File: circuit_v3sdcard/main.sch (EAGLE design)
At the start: 24 parts, among them CN1 SD, CN3 MICROSD, CN4 5035481020, IC1 C8051F381-GM, IC3 N25Q512A, IC4 KC2016K, IC6 MPU-9250

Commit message: Modified v3 circuit
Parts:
- removed D1, D2: (no value), diode:DIODE-SOD323-W
- removed LED1: (no value), LED:LED1608O
- removed R7: 10k, reg,cap:R-1005
- removed TP: PTR1TP10R, testpad:PTR1TP10R
- removed USB_GND: PTR1TP11R, testpad:PTR1TP11R
- D4: value (none) -> HSMS-2854; device diode:DIODE-SOD323-W -> avago:HSMS-2854
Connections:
- removed net N$15: IC1G$1.P2.7, R7.P$2, TP.TP
- removed net N$4: D1.C, D2.C, IC1G$1.REGIN
- removed net N$5: D4.C, IC1G$1.VBUS, R1.P$2
- removed net N$9: LED1.A, R7.P$1
- new net N$1: D4.C, IC1G$1.REGIN
- net +3V3: now also D4.A2; no longer D2.A
- net DGND: no longer LED1.K, USB_GND.TP
- net VBUS: now also D4.A1, IC1G$1.VBUS, R1.P$2; no longer D1.A, D4.A
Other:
- moved on the sheet: R1

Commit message: Fix parts positions
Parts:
- added C1: 1.0u, reg,cap:C-1005
- added R3: 100, reg,cap:R-1005
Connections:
- new net N$4: IC1G$1.VBUS, R3.P$1
- net DGND: now also C1.P$1
- net N$1: now also C1.P$2
- net VBUS: now also R3.P$2; no longer IC1G$1.VBUS
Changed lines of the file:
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@@
 <part name="SUPPLY1" library="supply2" deviceset="DGND" device=""/>
 <part name="D4" library="avago" library_urn="urn:adsk.eagle:library:107" deviceset="HSMS-2854" device="" package3d_urn="urn:adsk.eagle:package:4488/1"/>
+<part name="R3" library="reg,cap" deviceset="R-" device="1005" value="100"/>
+<part name="C1" library="reg,cap" deviceset="C-" device="1005" value="1.0u"/>
 </parts>
 <sheets>
@@
 <instance part="SUPPLY1" gate="G$1" x="-210.82" y="-60.96"/>
 <instance part="D4" gate="A" x="-48.26" y="-2.54" rot="MR180"/>
+<instance part="R3" gate="G$1" x="-40.64" y="-7.62" rot="R180"/>
+<instance part="C1" gate="G$1" x="-25.4" y="-22.86" rot="R90"/>
 </instances>
 <busses>
@@
 <pinref part="SUPPLY6" gate="G$1" pin="DGND"/>
 <pinref part="C6" gate="G$1" pin="P$1"/>
+<pinref part="C1" gate="G$1" pin="P$1"/>
+<wire x1="-30.48" y1="-27.94" x2="-25.4" y2="-27.94" width="0.1524" layer="91"/>
+<wire x1="-25.4" y1="-27.94" x2="-25.4" y2="-25.4" width="0.1524" layer="91"/>
 </segment>
 <segment>
@@
 <wire x1="-223.52" y1="-40.64" x2="-236.22" y2="-40.64" width="0.1524" layer="91"/>
 <label x="-233.68" y="-40.64" size="1.778" layer="95"/>
-<pinref part="IC1" gate="G$1" pin="VBUS"/>
 <pinref part="D3" gate="G$1" pin="4"/>
 <wire x1="-109.22" y1="-7.62" x2="-109.22" y2="-12.7" width="0.1524" layer="91"/>
@@
 <wire x1="-55.88" y1="-2.54" x2="-55.88" y2="-7.62" width="0.1524" layer="91"/>
 <junction x="-55.88" y="-7.62"/>
-<wire x1="-55.88" y1="-7.62" x2="-22.86" y2="-7.62" width="0.1524" layer="91"/>
+<wire x1="-55.88" y1="-7.62" x2="-45.72" y2="-7.62" width="0.1524" layer="91"/>
 <wire x1="-129.54" y1="-7.62" x2="-109.22" y2="-7.62" width="0.1524" layer="91"/>
 <junction x="-109.22" y="-7.62"/>
+<pinref part="R3" gate="G$1" pin="P$2"/>
 </segment>
 </net>
@@
 <pinref part="IC1" gate="G$1" pin="REGIN"/>
 <pinref part="D4" gate="A" pin="C"/>
-<wire x1="-48.26" y1="-5.08" x2="-22.86" y2="-5.08" width="0.1524" layer="91"/>
-</segment>
-</net>
+<wire x1="-48.26" y1="-5.08" x2="-25.4" y2="-5.08" width="0.1524" layer="91"/>
+<pinref part="C1" gate="G$1" pin="P$2"/>
+<wire x1="-25.4" y1="-5.08" x2="-22.86" y2="-5.08" width="0.1524" layer="91"/>
+<wire x1="-25.4" y1="-17.78" x2="-25.4" y2="-5.08" width="0.1524" layer="91"/>
+<junction x="-25.4" y="-5.08"/>
+</segment>
+</net>
+<net name="N$4" class="1">
+<segment>
+<pinref part="IC1" gate="G$1" pin="VBUS"/>
+<pinref part="R3" gate="G$1" pin="P$1"/>
+<wire x1="-38.1" y1="-7.62" x2="-22.86" y2="-7.62" width="0.1524" layer="91"/>
+</segment>
+</net>

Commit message: Added wiring
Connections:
- net D+: now also CN4.4; no longer CN4.6
- net D-: now also CN4.6; no longer CN4.4
- net GPIO0: now also IC1G$1.P2.6; no longer IC1G$1.P1.0
- net GPIO1: now also IC1G$1.P2.7; no longer IC1G$1.P1.1
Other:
- moved on the sheet: CN4

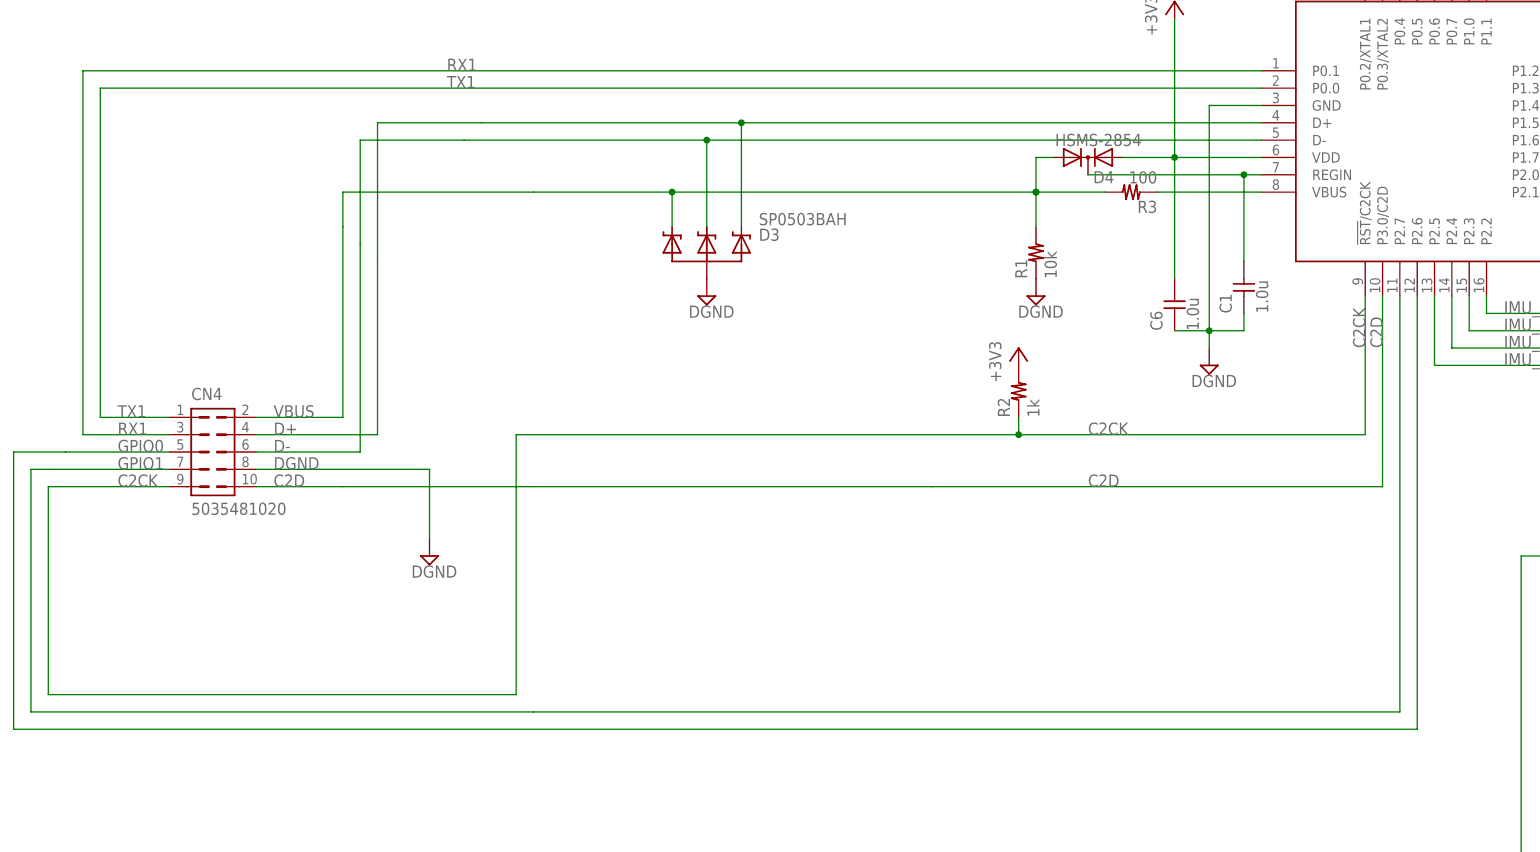
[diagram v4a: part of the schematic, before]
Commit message: Connected air wires
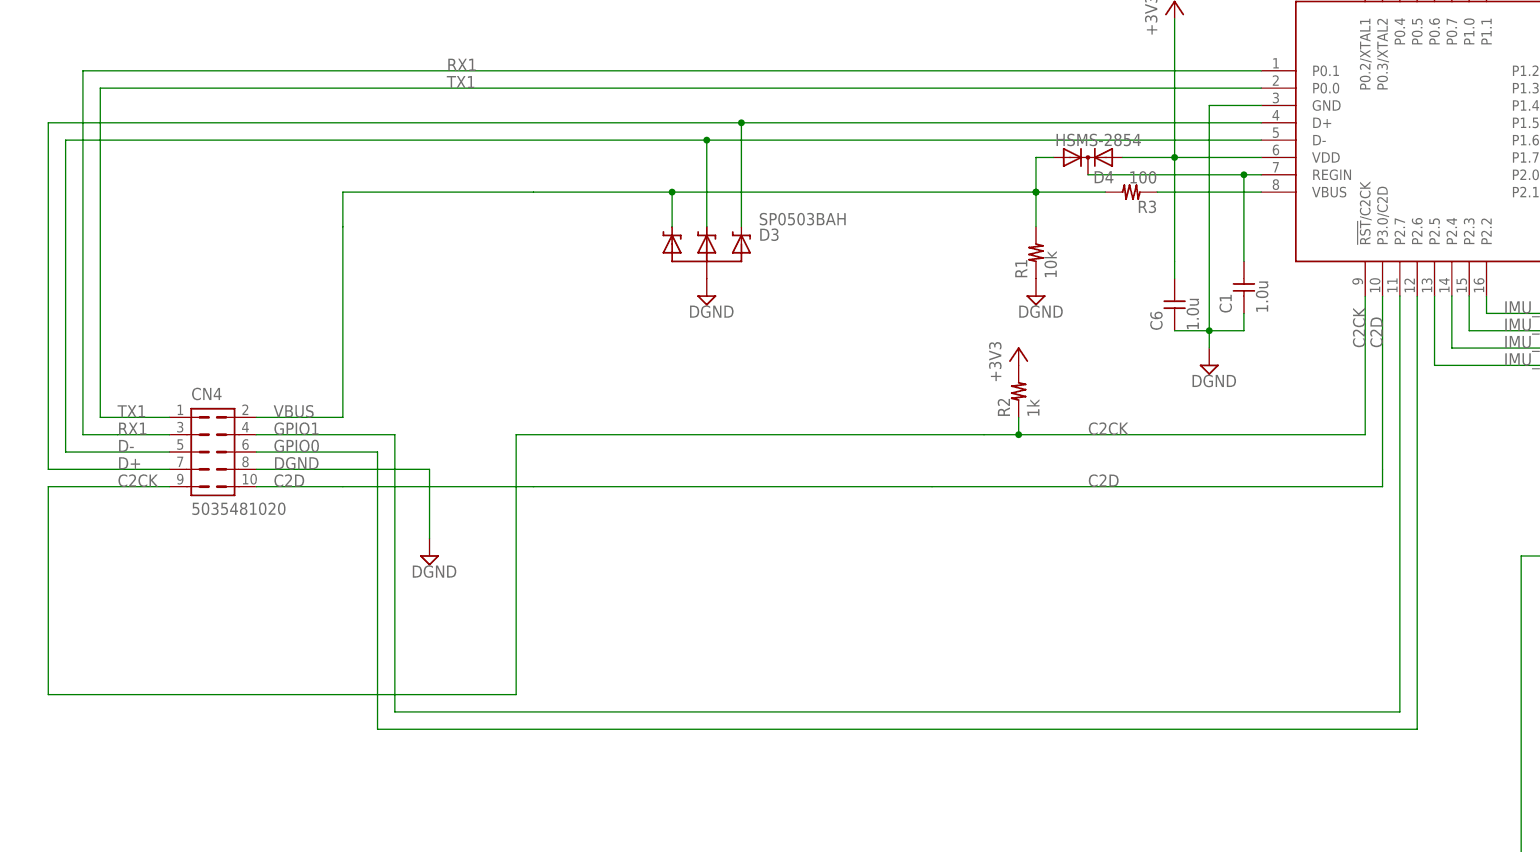
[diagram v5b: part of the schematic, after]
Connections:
- net D+: now also CN4.7; no longer CN4.4
- net D-: now also CN4.5; no longer CN4.6
- net GPIO0: now also CN4.6; no longer CN4.5
- net GPIO1: now also CN4.4; no longer CN4.7
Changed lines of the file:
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@@
 <segment>
 <wire x1="-22.86" y1="0" x2="-104.14" y2="0" width="0.1524" layer="91"/>
-<wire x1="-104.14" y1="0" x2="-139.7" y2="0" width="0.1524" layer="91"/>
-<wire x1="-154.94" y1="0" x2="-139.7" y2="0" width="0.1524" layer="91"/>
+<wire x1="-104.14" y1="0" x2="-198.12" y2="0" width="0.1524" layer="91"/>
 <wire x1="-104.14" y1="-12.7" x2="-104.14" y2="0" width="0.1524" layer="91"/>
 <junction x="-104.14" y="0"/>
 <pinref part="IC1" gate="G$1" pin="D-"/>
 <pinref part="D3" gate="G$1" pin="3"/>
-<wire x1="-154.94" y1="-43.18" x2="-154.94" y2="-15.24" width="0.1524" layer="91"/>
-<wire x1="-154.94" y1="-15.24" x2="-154.94" y2="0" width="0.1524" layer="91"/>
-<label x="-167.64" y="-45.72" size="1.778" layer="95"/>
-<wire x1="-154.94" y1="-43.18" x2="-154.94" y2="-45.72" width="0.1524" layer="91"/>
-<pinref part="CN4" gate="G$1" pin="6"/>
-<wire x1="-154.94" y1="-45.72" x2="-170.18" y2="-45.72" width="0.1524" layer="91"/>
+<label x="-190.5" y="-45.72" size="1.778" layer="95"/>
+<wire x1="-198.12" y1="0" x2="-198.12" y2="-45.72" width="0.1524" layer="91"/>
+<pinref part="CN4" gate="G$1" pin="5"/>
+<wire x1="-198.12" y1="-45.72" x2="-182.88" y2="-45.72" width="0.1524" layer="91"/>
 </segment>
 </net>
 <net name="D+" class="0">
 <segment>
-<wire x1="-137.16" y1="2.54" x2="-99.06" y2="2.54" width="0.1524" layer="91"/>
+<wire x1="-200.66" y1="2.54" x2="-99.06" y2="2.54" width="0.1524" layer="91"/>
 <wire x1="-99.06" y1="2.54" x2="-22.86" y2="2.54" width="0.1524" layer="91"/>
 <wire x1="-99.06" y1="-12.7" x2="-99.06" y2="2.54" width="0.1524" layer="91"/>
-<wire x1="-137.16" y1="2.54" x2="-152.4" y2="2.54" width="0.1524" layer="91"/>
 <junction x="-99.06" y="2.54"/>
 <pinref part="IC1" gate="G$1" pin="D+"/>
 <pinref part="D3" gate="G$1" pin="2"/>
-<wire x1="-152.4" y1="2.54" x2="-152.4" y2="-17.78" width="0.1524" layer="91"/>
-<wire x1="-152.4" y1="-17.78" x2="-152.4" y2="-43.18" width="0.1524" layer="91"/>
-<label x="-167.64" y="-43.18" size="1.778" layer="95"/>
-<pinref part="CN4" gate="G$1" pin="4"/>
-<wire x1="-170.18" y1="-43.18" x2="-152.4" y2="-43.18" width="0.1524" layer="91"/>
+<pinref part="CN4" gate="G$1" pin="7"/>
+<wire x1="-200.66" y1="2.54" x2="-200.66" y2="-48.26" width="0.1524" layer="91"/>
+<wire x1="-200.66" y1="-48.26" x2="-182.88" y2="-48.26" width="0.1524" layer="91"/>
+<label x="-190.5" y="-48.26" size="1.778" layer="95"/>
 </segment>
 </net>
@@
 <net name="GPIO0" class="0">
 <segment>
-<pinref part="CN4" gate="G$1" pin="5"/>
-<wire x1="-198.12" y1="-45.72" x2="-182.88" y2="-45.72" width="0.1524" layer="91"/>
-<label x="-190.5" y="-45.72" size="1.778" layer="95"/>
+<label x="-167.64" y="-45.72" size="1.778" layer="95"/>
 <pinref part="IC1" gate="G$1" pin="P2.6"/>
 <wire x1="0" y1="-22.86" x2="0" y2="-86.36" width="0.1524" layer="91"/>
-<wire x1="0" y1="-86.36" x2="-205.74" y2="-86.36" width="0.1524" layer="91"/>
-<wire x1="-205.74" y1="-86.36" x2="-205.74" y2="-45.72" width="0.1524" layer="91"/>
-<wire x1="-205.74" y1="-45.72" x2="-198.12" y2="-45.72" width="0.1524" layer="91"/>
+<wire x1="0" y1="-86.36" x2="-152.4" y2="-86.36" width="0.1524" layer="91"/>
+<pinref part="CN4" gate="G$1" pin="6"/>
+<wire x1="-152.4" y1="-86.36" x2="-152.4" y2="-45.72" width="0.1524" layer="91"/>
+<wire x1="-152.4" y1="-45.72" x2="-170.18" y2="-45.72" width="0.1524" layer="91"/>
 </segment>
 </net>
 <net name="GPIO1" class="0">
 <segment>
-<pinref part="CN4" gate="G$1" pin="7"/>
-<wire x1="-182.88" y1="-48.26" x2="-200.66" y2="-48.26" width="0.1524" layer="91"/>
-<label x="-190.5" y="-48.26" size="1.778" layer="95"/>
-<wire x1="-200.66" y1="-48.26" x2="-203.2" y2="-48.26" width="0.1524" layer="91"/>
-<wire x1="-203.2" y1="-48.26" x2="-203.2" y2="-83.82" width="0.1524" layer="91"/>
-<wire x1="-203.2" y1="-83.82" x2="-129.54" y2="-83.82" width="0.1524" layer="91"/>
+<label x="-167.64" y="-43.18" size="1.778" layer="95"/>
 <pinref part="IC1" gate="G$1" pin="P2.7"/>
-<wire x1="-129.54" y1="-83.82" x2="-2.54" y2="-83.82" width="0.1524" layer="91"/>
+<wire x1="-149.86" y1="-83.82" x2="-2.54" y2="-83.82" width="0.1524" layer="91"/>
 <wire x1="-2.54" y1="-83.82" x2="-2.54" y2="-22.86" width="0.1524" layer="91"/>
+<pinref part="CN4" gate="G$1" pin="4"/>
+<wire x1="-149.86" y1="-83.82" x2="-149.86" y2="-43.18" width="0.1524" layer="91"/>
+<wire x1="-149.86" y1="-43.18" x2="-170.18" y2="-43.18" width="0.1524" layer="91"/>
 </segment>
 </net>

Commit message: Modified circuit
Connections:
- net D+: now also CN4.5; no longer CN4.7
- net D-: now also CN4.3; no longer CN4.5
- net DGND: now also CN4.7; no longer CN4.8
- net GPIO0: now also CN4.8; no longer CN4.6
- net GPIO1: now also CN4.6; no longer CN4.4
- net RX1: now also CN4.4; no longer CN4.3
- net TX1: now also CN4.2; no longer CN4.1
- net VBUS: now also CN4.1; no longer CN4.2
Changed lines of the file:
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@@
 <instance part="R1" gate="G$1" x="-55.88" y="-17.78" rot="R90"/>
 <instance part="SUPPLY3" gate="G$1" x="-55.88" y="-22.86"/>
-<instance part="SUPPLY1" gate="G$1" x="-144.78" y="-60.96"/>
+<instance part="SUPPLY1" gate="G$1" x="-218.44" y="-50.8"/>
 <instance part="D4" gate="A" x="-48.26" y="-2.54" rot="MR180"/>
 <instance part="R3" gate="G$1" x="-40.64" y="-7.62" rot="R180"/>
@@
 </segment>
 <segment>
-<pinref part="CN4" gate="G$1" pin="8"/>
-<wire x1="-170.18" y1="-48.26" x2="-144.78" y2="-48.26" width="0.1524" layer="91"/>
-<wire x1="-144.78" y1="-48.26" x2="-144.78" y2="-58.42" width="0.1524" layer="91"/>
 <pinref part="SUPPLY1" gate="G$1" pin="DGND"/>
-<label x="-167.64" y="-48.26" size="1.778" layer="95"/>
+<label x="-190.5" y="-40.64" size="1.778" layer="95"/>
+<pinref part="CN4" gate="G$1" pin="7"/>
+<wire x1="-182.88" y1="-48.26" x2="-218.44" y2="-48.26" width="0.1524" layer="91"/>
 </segment>
 </net>
@@
 <pinref part="IC1" gate="G$1" pin="D-"/>
 <pinref part="D3" gate="G$1" pin="3"/>
-<label x="-190.5" y="-45.72" size="1.778" layer="95"/>
-<wire x1="-198.12" y1="0" x2="-198.12" y2="-45.72" width="0.1524" layer="91"/>
-<pinref part="CN4" gate="G$1" pin="5"/>
-<wire x1="-198.12" y1="-45.72" x2="-182.88" y2="-45.72" width="0.1524" layer="91"/>
+<label x="-190.5" y="-43.18" size="1.778" layer="95"/>
+<wire x1="-198.12" y1="0" x2="-198.12" y2="-43.18" width="0.1524" layer="91"/>
+<pinref part="CN4" gate="G$1" pin="3"/>
+<wire x1="-198.12" y1="-43.18" x2="-182.88" y2="-43.18" width="0.1524" layer="91"/>
 </segment>
 </net>
@@
 <pinref part="IC1" gate="G$1" pin="D+"/>
 <pinref part="D3" gate="G$1" pin="2"/>
-<pinref part="CN4" gate="G$1" pin="7"/>
-<wire x1="-200.66" y1="2.54" x2="-200.66" y2="-48.26" width="0.1524" layer="91"/>
-<wire x1="-200.66" y1="-48.26" x2="-182.88" y2="-48.26" width="0.1524" layer="91"/>
-<label x="-190.5" y="-48.26" size="1.778" layer="95"/>
+<wire x1="-200.66" y1="2.54" x2="-200.66" y2="-45.72" width="0.1524" layer="91"/>
+<label x="-190.5" y="-45.72" size="1.778" layer="95"/>
+<pinref part="CN4" gate="G$1" pin="5"/>
+<wire x1="-200.66" y1="-45.72" x2="-182.88" y2="-45.72" width="0.1524" layer="91"/>
 </segment>
 </net>
@@
 <net name="VBUS" class="1">
 <segment>
-<wire x1="-129.54" y1="-7.62" x2="-157.48" y2="-7.62" width="0.1524" layer="91"/>
-<wire x1="-157.48" y1="-7.62" x2="-157.48" y2="-12.7" width="0.1524" layer="91"/>
-<wire x1="-157.48" y1="-12.7" x2="-157.48" y2="-40.64" width="0.1524" layer="91"/>
-<pinref part="CN4" gate="G$1" pin="2"/>
-<wire x1="-157.48" y1="-40.64" x2="-170.18" y2="-40.64" width="0.1524" layer="91"/>
-<label x="-167.64" y="-40.64" size="1.778" layer="95"/>
+<wire x1="-109.22" y1="-7.62" x2="-157.48" y2="-7.62" width="0.1524" layer="91"/>
+<wire x1="-157.48" y1="-7.62" x2="-157.48" y2="-38.1" width="0.1524" layer="91"/>
+<label x="-190.5" y="-48.26" size="1.778" layer="95"/>
 <pinref part="D3" gate="G$1" pin="4"/>
 <wire x1="-109.22" y1="-7.62" x2="-109.22" y2="-12.7" width="0.1524" layer="91"/>
@@
 <junction x="-55.88" y="-7.62"/>
 <wire x1="-55.88" y1="-7.62" x2="-45.72" y2="-7.62" width="0.1524" layer="91"/>
-<wire x1="-129.54" y1="-7.62" x2="-109.22" y2="-7.62" width="0.1524" layer="91"/>
 <junction x="-109.22" y="-7.62"/>
 <pinref part="R3" gate="G$1" pin="P$2"/>
+<pinref part="CN4" gate="G$1" pin="1"/>
+<wire x1="-182.88" y1="-38.1" x2="-157.48" y2="-38.1" width="0.1524" layer="91"/>
+<wire x1="-182.88" y1="-40.64" x2="-182.88" y2="-38.1" width="0.1524" layer="91"/>
 </segment>
 </net>
@@
 <pinref part="IC1" gate="G$1" pin="P0.1"/>
 <wire x1="-22.86" y1="10.16" x2="-195.58" y2="10.16" width="0.1524" layer="91"/>
-<wire x1="-195.58" y1="10.16" x2="-195.58" y2="-43.18" width="0.1524" layer="91"/>
+<wire x1="-195.58" y1="10.16" x2="-195.58" y2="-22.86" width="0.1524" layer="91"/>
 <label x="-142.24" y="10.16" size="1.778" layer="95"/>
-<pinref part="CN4" gate="G$1" pin="3"/>
-<wire x1="-182.88" y1="-43.18" x2="-190.5" y2="-43.18" width="0.1524" layer="91"/>
-<wire x1="-190.5" y1="-43.18" x2="-195.58" y2="-43.18" width="0.1524" layer="91"/>
-<label x="-190.5" y="-43.18" size="1.778" layer="95"/>
+<label x="-167.64" y="-43.18" size="1.778" layer="95"/>
+<wire x1="-195.58" y1="-22.86" x2="-154.94" y2="-22.86" width="0.1524" layer="91"/>
+<wire x1="-154.94" y1="-22.86" x2="-154.94" y2="-43.18" width="0.1524" layer="91"/>
+<pinref part="CN4" gate="G$1" pin="4"/>
+<wire x1="-154.94" y1="-43.18" x2="-170.18" y2="-43.18" width="0.1524" layer="91"/>
 </segment>
 </net>
@@
 <wire x1="-193.04" y1="7.62" x2="-22.86" y2="7.62" width="0.1524" layer="91"/>
 <label x="-142.24" y="7.62" size="1.778" layer="95"/>
-<pinref part="CN4" gate="G$1" pin="1"/>
-<wire x1="-182.88" y1="-40.64" x2="-193.04" y2="-40.64" width="0.1524" layer="91"/>
-<wire x1="-193.04" y1="-40.64" x2="-193.04" y2="7.62" width="0.1524" layer="91"/>
-<label x="-190.5" y="-40.64" size="1.778" layer="95"/>
+<label x="-167.64" y="-40.64" size="1.778" layer="95"/>
+<wire x1="-193.04" y1="-20.32" x2="-193.04" y2="7.62" width="0.1524" layer="91"/>
+<wire x1="-193.04" y1="-20.32" x2="-152.4" y2="-20.32" width="0.1524" layer="91"/>
+<wire x1="-152.4" y1="-20.32" x2="-152.4" y2="-40.64" width="0.1524" layer="91"/>
+<pinref part="CN4" gate="G$1" pin="2"/>
+<wire x1="-170.18" y1="-40.64" x2="-152.4" y2="-40.64" width="0.1524" layer="91"/>
 </segment>
 </net>
 <net name="GPIO0" class="0">
 <segment>
-<label x="-167.64" y="-45.72" size="1.778" layer="95"/>
+<label x="-167.64" y="-48.26" size="1.778" layer="95"/>
 <pinref part="IC1" gate="G$1" pin="P2.6"/>
 <wire x1="0" y1="-22.86" x2="0" y2="-86.36" width="0.1524" layer="91"/>
 <wire x1="0" y1="-86.36" x2="-152.4" y2="-86.36" width="0.1524" layer="91"/>
-<pinref part="CN4" gate="G$1" pin="6"/>
-<wire x1="-152.4" y1="-86.36" x2="-152.4" y2="-45.72" width="0.1524" layer="91"/>
-<wire x1="-152.4" y1="-45.72" x2="-170.18" y2="-45.72" width="0.1524" layer="91"/>
+<wire x1="-152.4" y1="-86.36" x2="-152.4" y2="-48.26" width="0.1524" layer="91"/>
+<pinref part="CN4" gate="G$1" pin="8"/>
+<wire x1="-170.18" y1="-48.26" x2="-152.4" y2="-48.26" width="0.1524" layer="91"/>
 </segment>
 </net>
 <net name="GPIO1" class="0">
 <segment>
-<label x="-167.64" y="-43.18" size="1.778" layer="95"/>
+<label x="-167.64" y="-45.72" size="1.778" layer="95"/>
 <pinref part="IC1" gate="G$1" pin="P2.7"/>
 <wire x1="-149.86" y1="-83.82" x2="-2.54" y2="-83.82" width="0.1524" layer="91"/>
 <wire x1="-2.54" y1="-83.82" x2="-2.54" y2="-22.86" width="0.1524" layer="91"/>
-<pinref part="CN4" gate="G$1" pin="4"/>
-<wire x1="-149.86" y1="-83.82" x2="-149.86" y2="-43.18" width="0.1524" layer="91"/>
-<wire x1="-149.86" y1="-43.18" x2="-170.18" y2="-43.18" width="0.1524" layer="91"/>
-</segment>
-</net>
+<wire x1="-149.86" y1="-83.82" x2="-149.86" y2="-45.72" width="0.1524" layer="91"/>
+<pinref part="CN4" gate="G$1" pin="6"/>
+<wire x1="-170.18" y1="-45.72" x2="-149.86" y2="-45.72" width="0.1524" layer="91"/>
+</segment>
+</net>
